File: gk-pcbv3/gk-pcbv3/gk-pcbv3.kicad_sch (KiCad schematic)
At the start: 39 parts, among them J1 USB_C_Receptacle_USB2.0, J14 USB_A, J2 Conn_01x02, J7 Conn_01x02, J8 Conn_ARM_JTAG_SWD_10, U1 WE-TVS-82400102, U10 MAX17048, U21 BQ24075RGT (_not_ BQ24075*T*R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, U23 WE-TVS-82400102, U24 TPS2051CDBV

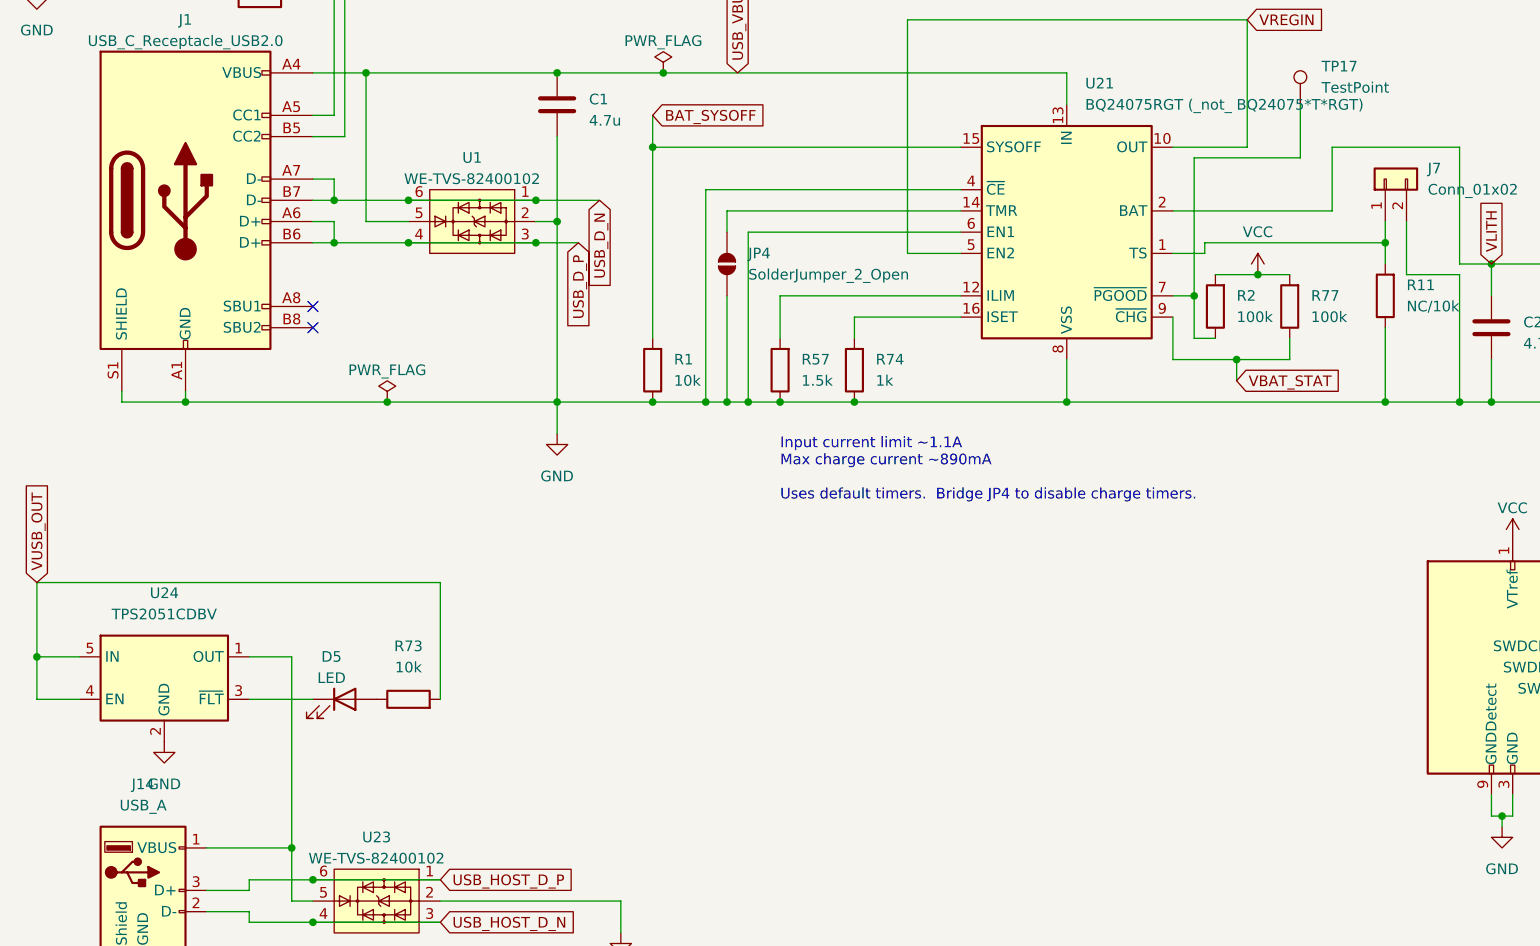
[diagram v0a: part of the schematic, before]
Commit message: Add TODOs to schematic Update to Kicad 9
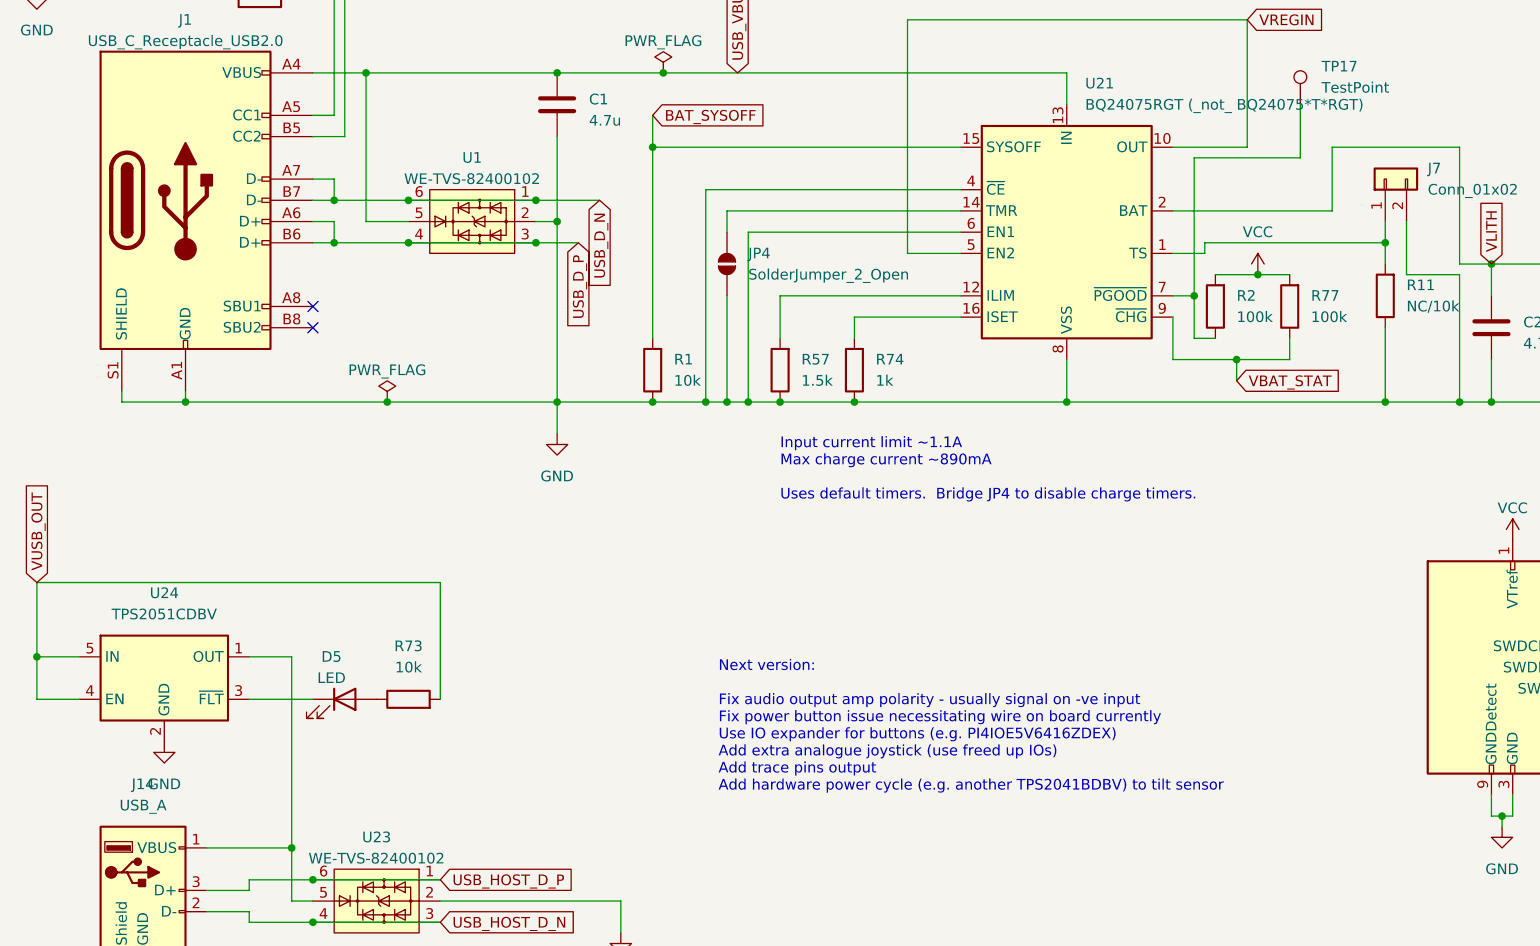
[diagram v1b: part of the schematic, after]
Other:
- note added: "Next version: Fix audio output amp polarity - usually signal on -ve input Fix power button issue necessitating wire on board currently Use IO expander for buttons (e.g. PI4IOE5V6416ZDEX) Add extra analogue joystick (use freed up IOs) Add trace pins output Add hardware power cycle (e.g. another TPS2041BDBV) to tilt sensor"
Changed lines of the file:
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@@
 (kicad_sch
-	(version 20231120)
+	(version 20250114)
 	(generator "eeschema")
-	(generator_version "8.0")
+	(generator_version "9.0")
 	(paper "A4")
+	(text "Hotplate profile:\n\nSMD291SNL: 160C 3 minutes, 260C 2 minutes.\nSMD291AX:  140C 3 minutes, 240C 2 minutes."
+		(exclude_from_sim no)
+		(at 177.8 155.194 0)
+		(effects
+			(font
+				(size 1.27 1.27)
+			)
+			(justify left)
+		)
+	)
+	(text "Next version:\n\nFix audio output amp polarity - usually signal on -ve input\nFix power button issue necessitating wire on board currently\nUse IO expander for buttons (e.g. PI4IOE5V6416ZDEX)\nAdd extra analogue joystick (use freed up IOs)\nAdd trace pins output\nAdd hardware power cycle (e.g. another TPS2041BDBV) to tilt sensor"
+		(exclude_from_sim no)
+		(at 100.584 111.252 0)
+		(effects
+			(font
+				(size 1.27 1.27)
+			)
+			(justify left)
+		)
+	)
+	(text "Input current limit ~1.1A\nMax charge current ~890mA\n\nUses default timers.  Bridge JP4 to disable charge timers."
+		(exclude_from_sim no)
+		(at 107.95 80.518 0)
+		(effects
+			(font
+				(size 1.27 1.27)
+			)
+			(justify left)
+		)
+	)
 	(junction
 		(at 93.98 33.02)
@@
 		)
 	)
-	(text "Hotplate profile:\n\nSMD291SNL: 160C 3 minutes, 260C 2 minutes.\nSMD291AX:  140C 3 minutes, 240C 2 minutes."
-		(exclude_from_sim no)
-		(at 177.8 155.194 0)
-		(effects
-			(font
-				(size 1.27 1.27)
-			)
-			(justify left)
-		)
-	)
-	(text "Input current limit ~1.1A\nMax charge current ~890mA\n\nUses default timers.  Bridge JP4 to disable charge timers."
-		(exclude_from_sim no)
-		(at 107.95 80.518 0)
-		(effects
-			(font
-				(size 1.27 1.27)
-			)
-			(justify left)
-		)
-	)
 	(global_label "USB_D_P"
 		(shape input)
@@
 		(at 92.71 171.45)
 		(size 12.7 19.05)
+		(exclude_from_sim no)
+		(in_bom yes)
+		(on_board yes)
+		(dnp no)
 		(fields_autoplaced yes)
 		(stroke
@@
 		(at 64.77 149.86)
 		(size 12.7 15.24)
+		(exclude_from_sim no)
+		(in_bom yes)
+		(on_board yes)
+		(dnp no)
 		(fields_autoplaced yes)
 		(stroke
@@
 		(at 88.9 151.13)
 		(size 16.51 15.24)
+		(exclude_from_sim no)
+		(in_bom yes)
+		(on_board yes)
+		(dnp no)
 		(fields_autoplaced yes)
 		(stroke
@@
 		(at 113.03 151.13)
 		(size 15.24 13.97)
+		(exclude_from_sim no)
+		(in_bom yes)
+		(on_board yes)
+		(dnp no)
 		(fields_autoplaced yes)
 		(stroke
@@
 		(at 66.04 171.45)
 		(size 13.97 19.05)
+		(exclude_from_sim no)
+		(in_bom yes)
+		(on_board yes)
+		(dnp no)
 		(fields_autoplaced yes)
 		(stroke
@@
 		(at 20.32 171.45)
 		(size 15.24 19.05)
+		(exclude_from_sim no)
+		(in_bom yes)
+		(on_board yes)
+		(dnp no)
 		(fields_autoplaced yes)
 		(stroke
@@
 		(at 41.91 171.45)
 		(size 15.24 19.05)
+		(exclude_from_sim no)
+		(in_bom yes)
+		(on_board yes)
+		(dnp no)
 		(fields_autoplaced yes)
 		(stroke
@@
 		(at 115.57 171.45)
 		(size 12.7 19.05)
+		(exclude_from_sim no)
+		(in_bom yes)
+		(on_board yes)
+		(dnp no)
 		(fields_autoplaced yes)
 		(stroke
@@
 		)
 	)
+	(embedded_fonts no)
 )
